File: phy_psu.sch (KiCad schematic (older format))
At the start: 53 parts, among them U4 88E1545

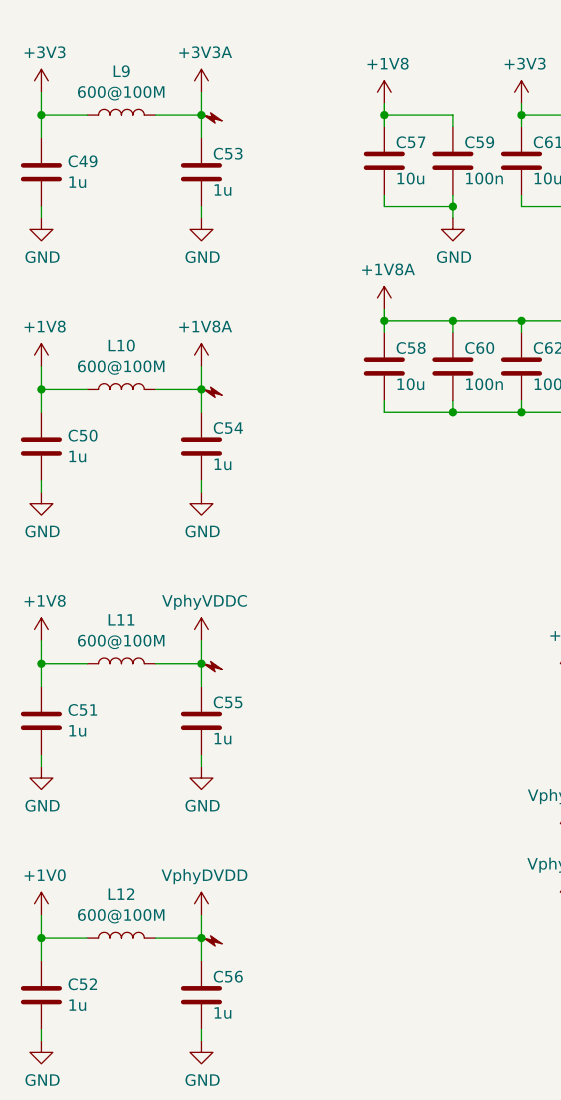
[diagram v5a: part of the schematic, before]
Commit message: sch, pcb: Add testpads on lots of signals
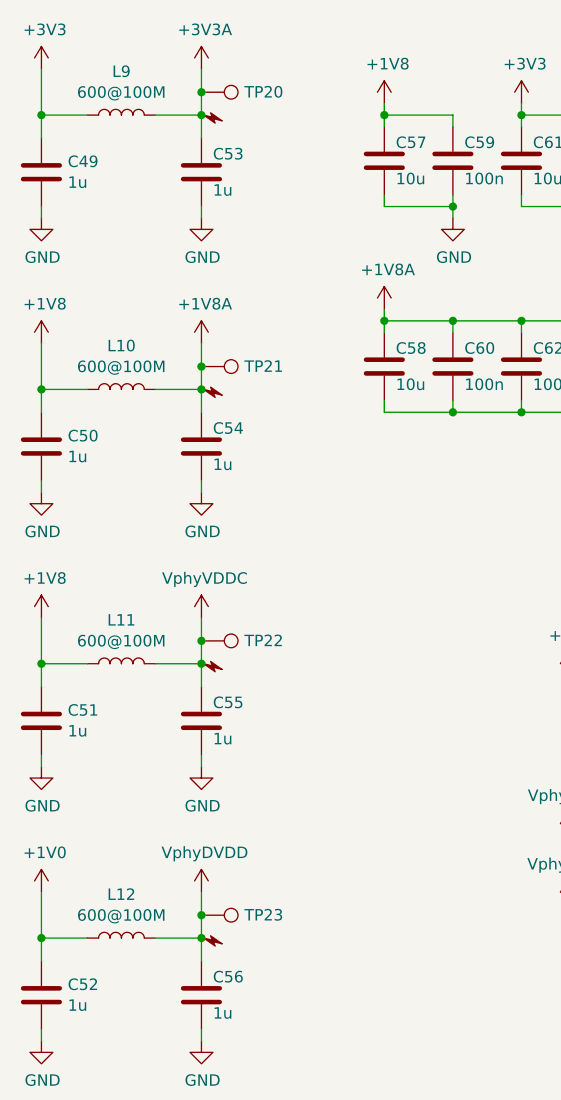
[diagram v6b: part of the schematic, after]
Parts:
- added TP20, TP21, TP22, TP23: TestPoint, TestPoint:TestPoint_Pad_D1.0mm, symbol Connector:TestPoint
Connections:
- net +1V8A: now also TP21.1
- net +3V3A: now also TP20.1
- net VphyDVDD: now also TP23.1
- net VphyVDDC: now also TP22.1
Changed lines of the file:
@@
 L power:+3V3 #PWR?
 U 1 1 5CA822F7
-P 1700 1500
+P 1700 1400
 AR Path="/5C7D0D1E/5C7D3CAF/5CA822F7" Ref="#PWR?"  Part="1"
 AR Path="/5C7D0D1E/5C7D3CB2/5CA822F7" Ref="#PWR?"  Part="1"
 AR Path="/5D05A5E3/5CA822F7" Ref="#PWR0115"  Part="1"
-F 0 "#PWR0115" H 1700 1350 50  0001 C CNN
-F 1 "+3V3" H 1715 1673 50  0000 C CNN
-F 2 "" H 1700 1500 50  0001 C CNN
-F 3 "" H 1700 1500 50  0001 C CNN
-	1    1700 1500
-	1    0    0    -1
-$EndComp
-Wire Wire Line
-	1700 1500 1700 1600
+F 0 "#PWR0115" H 1700 1250 50  0001 C CNN
+F 1 "+3V3" H 1715 1573 50  0000 C CNN
+F 2 "" H 1700 1400 50  0001 C CNN
+F 3 "" H 1700 1400 50  0001 C CNN
+	1    1700 1400
+	1    0    0    -1
+$EndComp
+Wire Wire Line
+	1700 1400 1700 1600
 Connection ~ 1700 1600
 Wire Wire Line
@@
 	1    0    0    -1
 $EndComp
-$Comp
-L pimouss-motherboard:+3V3A #PWR0123
-U 1 1 5CA8AACC
-P 2400 1500
-F 0 "#PWR0123" H 2400 1350 50  0001 C CNN
-F 1 "+3V3A" H 2415 1673 50  0000 C CNN
-F 2 "" H 2400 1500 50  0001 C CNN
-F 3 "" H 2400 1500 50  0001 C CNN
-	1    2400 1500
-	1    0    0    -1
-$EndComp
-Wire Wire Line
-	2400 1500 2400 1600
 Connection ~ 2400 1600
 $Comp
@@
 	1700 2800 1700 2900
 Wire Wire Line
-	1700 2700 1700 2800
+	1700 2600 1700 2800
 Connection ~ 1700 2800
 Wire Wire Line
@@
 $EndComp
 Wire Wire Line
-	2400 2700 2400 2800
+	2400 2600 2400 2700
 Connection ~ 2400 2800
 $Comp
 L pimouss-motherboard:+1V8A #PWR0125
 U 1 1 5CA94250
-P 2400 2700
-F 0 "#PWR0125" H 2400 2550 50  0001 C CNN
-F 1 "+1V8A" H 2415 2873 50  0000 C CNN
-F 2 "" H 2400 2700 50  0001 C CNN
-F 3 "" H 2400 2700 50  0001 C CNN
-	1    2400 2700
+P 2400 2600
+F 0 "#PWR0125" H 2400 2450 50  0001 C CNN
+F 1 "+1V8A" H 2415 2773 50  0000 C CNN
+F 2 "" H 2400 2600 50  0001 C CNN
+F 3 "" H 2400 2600 50  0001 C CNN
+	1    2400 2600
 	1    0    0    -1
 $EndComp
@@
 L power:+1V8 #PWR0117
 U 1 1 5CA9429E
-P 1700 2700
-F 0 "#PWR0117" H 1700 2550 50  0001 C CNN
-F 1 "+1V8" H 1715 2873 50  0000 C CNN
-F 2 "" H 1700 2700 50  0001 C CNN
-F 3 "" H 1700 2700 50  0001 C CNN
-	1    1700 2700
+P 1700 2600
+F 0 "#PWR0117" H 1700 2450 50  0001 C CNN
+F 1 "+1V8" H 1715 2773 50  0000 C CNN
+F 2 "" H 1700 2600 50  0001 C CNN
+F 3 "" H 1700 2600 50  0001 C CNN
+	1    1700 2600
 	1    0    0    -1
 $EndComp
@@
 	1700 4000 1700 4100
 Wire Wire Line
-	1700 3900 1700 4000
+	1700 3800 1700 4000
 Connection ~ 1700 4000
 Wire Wire Line
@@
 $EndComp
 Wire Wire Line
-	2400 3900 2400 4000
+	2400 3800 2400 3900
 Connection ~ 2400 4000
 $Comp
 L power:+1V8 #PWR0119
 U 1 1 5CA943F8
-P 1700 3900
-F 0 "#PWR0119" H 1700 3750 50  0001 C CNN
-F 1 "+1V8" H 1715 4073 50  0000 C CNN
-F 2 "" H 1700 3900 50  0001 C CNN
-F 3 "" H 1700 3900 50  0001 C CNN
-	1    1700 3900
+P 1700 3800
+F 0 "#PWR0119" H 1700 3650 50  0001 C CNN
+F 1 "+1V8" H 1715 3973 50  0000 C CNN
+F 2 "" H 1700 3800 50  0001 C CNN
+F 3 "" H 1700 3800 50  0001 C CNN
+	1    1700 3800
 	1    0    0    -1
 $EndComp
@@
 L pimouss-motherboard:VphyVDDC #PWR0127
 U 1 1 5CA9A97E
-P 2400 3900
-F 0 "#PWR0127" H 2400 3750 50  0001 C CNN
-F 1 "VphyVDDC" H 2415 4073 50  0000 C CNN
-F 2 "" H 2400 3900 50  0001 C CNN
-F 3 "" H 2400 3900 50  0001 C CNN
-	1    2400 3900
+P 2400 3800
+F 0 "#PWR0127" H 2400 3650 50  0001 C CNN
+F 1 "VphyVDDC" H 2415 3973 50  0000 C CNN
+F 2 "" H 2400 3800 50  0001 C CNN
+F 3 "" H 2400 3800 50  0001 C CNN
+	1    2400 3800
 	1    0    0    -1
 $EndComp
@@
 	1700 5200 1700 5300
 Wire Wire Line
-	1700 5100 1700 5200
+	1700 5000 1700 5200
 Connection ~ 1700 5200
 Wire Wire Line
@@
 $EndComp
 Wire Wire Line
-	2400 5100 2400 5200
+	2400 5000 2400 5100
 Connection ~ 2400 5200
 $Comp
 L pimouss-motherboard:VphyDVDD #PWR0129
 U 1 1 5CAA2562
-P 2400 5100
-F 0 "#PWR0129" H 2400 4950 50  0001 C CNN
-F 1 "VphyDVDD" H 2415 5273 50  0000 C CNN
-F 2 "" H 2400 5100 50  0001 C CNN
-F 3 "" H 2400 5100 50  0001 C CNN
-	1    2400 5100
+P 2400 5000
+F 0 "#PWR0129" H 2400 4850 50  0001 C CNN
+F 1 "VphyDVDD" H 2415 5173 50  0000 C CNN
+F 2 "" H 2400 5000 50  0001 C CNN
+F 3 "" H 2400 5000 50  0001 C CNN
+	1    2400 5000
 	1    0    0    -1
 $EndComp
@@
 L power:+1V0 #PWR0121
 U 1 1 5CAA25B5
-P 1700 5100
-F 0 "#PWR0121" H 1700 4950 50  0001 C CNN
-F 1 "+1V0" H 1715 5273 50  0000 C CNN
-F 2 "" H 1700 5100 50  0001 C CNN
-F 3 "" H 1700 5100 50  0001 C CNN
-	1    1700 5100
+P 1700 5000
+F 0 "#PWR0121" H 1700 4850 50  0001 C CNN
+F 1 "+1V0" H 1715 5173 50  0000 C CNN
+F 2 "" H 1700 5000 50  0001 C CNN
+F 3 "" H 1700 5000 50  0001 C CNN
+	1    1700 5000
 	1    0    0    -1
 $EndComp
@@
 	0    1    1    0
 $EndComp
+Wire Wire Line
+	2400 1400 2400 1500
+$Comp
+L pimouss-motherboard:+3V3A #PWR0123
+U 1 1 5CA8AACC
+P 2400 1400
+F 0 "#PWR0123" H 2400 1250 50  0001 C CNN
+F 1 "+3V3A" H 2415 1573 50  0000 C CNN
+F 2 "" H 2400 1400 50  0001 C CNN
+F 3 "" H 2400 1400 50  0001 C CNN
+	1    2400 1400
+	1    0    0    -1
+$EndComp
+$Comp
+L Connector:TestPoint TP?
+U 1 1 5D48259C
+P 2400 5100
+AR Path="/5D05A5E1/5D48259C" Ref="TP?"  Part="1"
+AR Path="/5CE77C37/5D48259C" Ref="TP?"  Part="1"
+AR Path="/5D05A5E3/5D48259C" Ref="TP23"  Part="1"
+F 0 "TP23" V 2400 5288 50  0000 L CNN
+F 1 "TestPoint" V 2445 5288 50  0001 L CNN
+F 2 "TestPoint:TestPoint_Pad_D1.0mm" H 2600 5100 50  0001 C CNN
+F 3 "~" H 2600 5100 50  0001 C CNN
+	1    2400 5100
+	0    1    1    0
+$EndComp
+Connection ~ 2400 5100
+Wire Wire Line
+	2400 5100 2400 5200
+$Comp
+L Connector:TestPoint TP?
+U 1 1 5D4BD5B0
+P 2400 3900
+AR Path="/5D05A5E1/5D4BD5B0" Ref="TP?"  Part="1"
+AR Path="/5CE77C37/5D4BD5B0" Ref="TP?"  Part="1"
+AR Path="/5D05A5E3/5D4BD5B0" Ref="TP22"  Part="1"
+F 0 "TP22" V 2400 4088 50  0000 L CNN
+F 1 "TestPoint" V 2445 4088 50  0001 L CNN
+F 2 "TestPoint:TestPoint_Pad_D1.0mm" H 2600 3900 50  0001 C CNN
+F 3 "~" H 2600 3900 50  0001 C CNN
+	1    2400 3900
+	0    1    1    0
+$EndComp
+Connection ~ 2400 3900
+Wire Wire Line
+	2400 3900 2400 4000
+$Comp
+L Connector:TestPoint TP?
+U 1 1 5D4BE08E
+P 2400 2700
+AR Path="/5D05A5E1/5D4BE08E" Ref="TP?"  Part="1"
+AR Path="/5CE77C37/5D4BE08E" Ref="TP?"  Part="1"
+AR Path="/5D05A5E3/5D4BE08E" Ref="TP21"  Part="1"
+F 0 "TP21" V 2400 2888 50  0000 L CNN
+F 1 "TestPoint" V 2445 2888 50  0001 L CNN
+F 2 "TestPoint:TestPoint_Pad_D1.0mm" H 2600 2700 50  0001 C CNN
+F 3 "~" H 2600 2700 50  0001 C CNN
+	1    2400 2700
+	0    1    1    0
+$EndComp
+Connection ~ 2400 2700
+Wire Wire Line
+	2400 2700 2400 2800
+$Comp
+L Connector:TestPoint TP?
+U 1 1 5D4BE8C9
+P 2400 1500
+AR Path="/5D05A5E1/5D4BE8C9" Ref="TP?"  Part="1"
+AR Path="/5CE77C37/5D4BE8C9" Ref="TP?"  Part="1"
+AR Path="/5D05A5E3/5D4BE8C9" Ref="TP20"  Part="1"
+F 0 "TP20" V 2400 1688 50  0000 L CNN
+F 1 "TestPoint" V 2445 1688 50  0001 L CNN
+F 2 "TestPoint:TestPoint_Pad_D1.0mm" H 2600 1500 50  0001 C CNN
+F 3 "~" H 2600 1500 50  0001 C CNN
+	1    2400 1500
+	0    1    1    0
+$EndComp
+Connection ~ 2400 1500
+Wire Wire Line
+	2400 1500 2400 1600
 $EndSCHEMATC
